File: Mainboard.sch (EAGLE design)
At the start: 80 parts, among them J1 POWER_JACKPTH_LOCK, T1 MOSFET_PCHAN_20A, T10 SINGLE_NCHAN_FET, T2 SINGLE_NCHAN_FET, T3 MOSFET_PCHAN_20A, T4 SINGLE_NCHAN_FET, T5 MOSFET_PCHAN_20A, T6 SINGLE_NCHAN_FET, T7 MOSFET_PCHAN_20A, T8 SINGLE_NCHAN_FET, T9 MOSFET_PCHAN_20A, U1 RFM23BP, U2 ARDUINO_PRO_MINI, U3 HMC5883LSMD, U4 TEENSY_3.0+4, U5 ITG-3200, U6 CURRENT_MAX4372, U7 MURATA_REG_OKL-T3-W12, U8 CURRENT_MAX4372

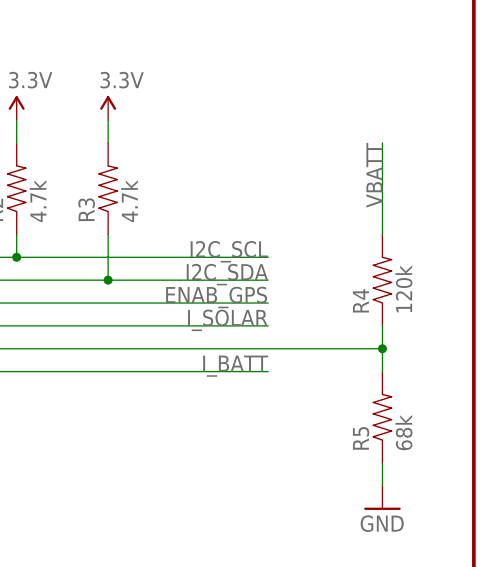
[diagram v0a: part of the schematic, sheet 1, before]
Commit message: Changed R4 value on mainboard
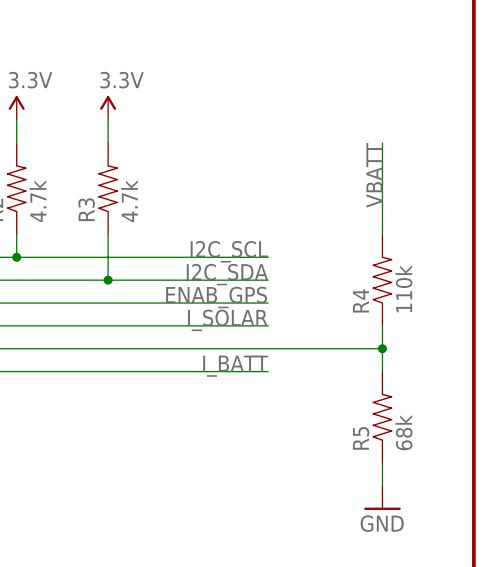
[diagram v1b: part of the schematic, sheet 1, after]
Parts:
- R4: value 120k -> 110k
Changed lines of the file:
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@@
 <part name="P+4" library="SparkFun" deviceset="3.3V" device=""/>
 <part name="P+6" library="SparkFun" deviceset="3.3V" device=""/>
-<part name="R4" library="SparkFun-Resistors" deviceset="RESISTOR" device="0805-RES" value="120k"/>
+<part name="R4" library="SparkFun-Resistors" deviceset="RESISTOR" device="0805-RES" value="110k"/>
 <part name="R5" library="SparkFun-Resistors" deviceset="RESISTOR" device="0805-RES" value="68k"/>
 <part name="GND28" library="SparkFun" deviceset="GND" device=""/>

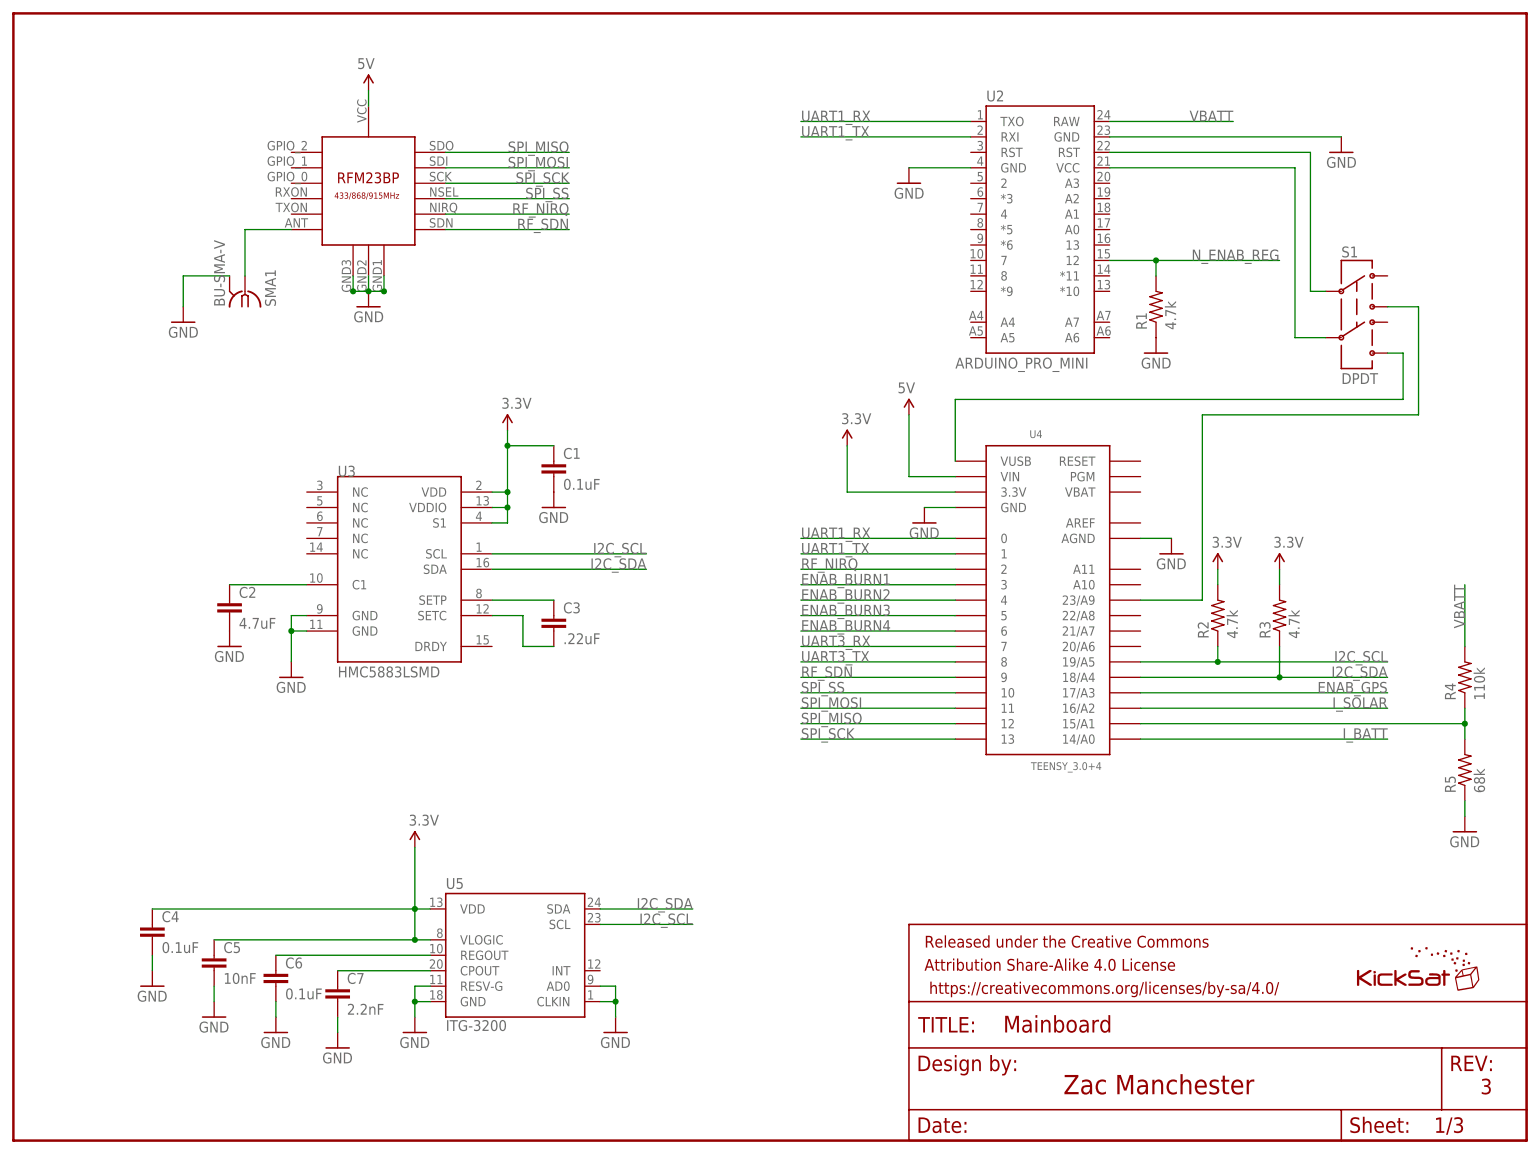
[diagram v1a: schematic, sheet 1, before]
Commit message: Added cap to battery voltage divider ADC input
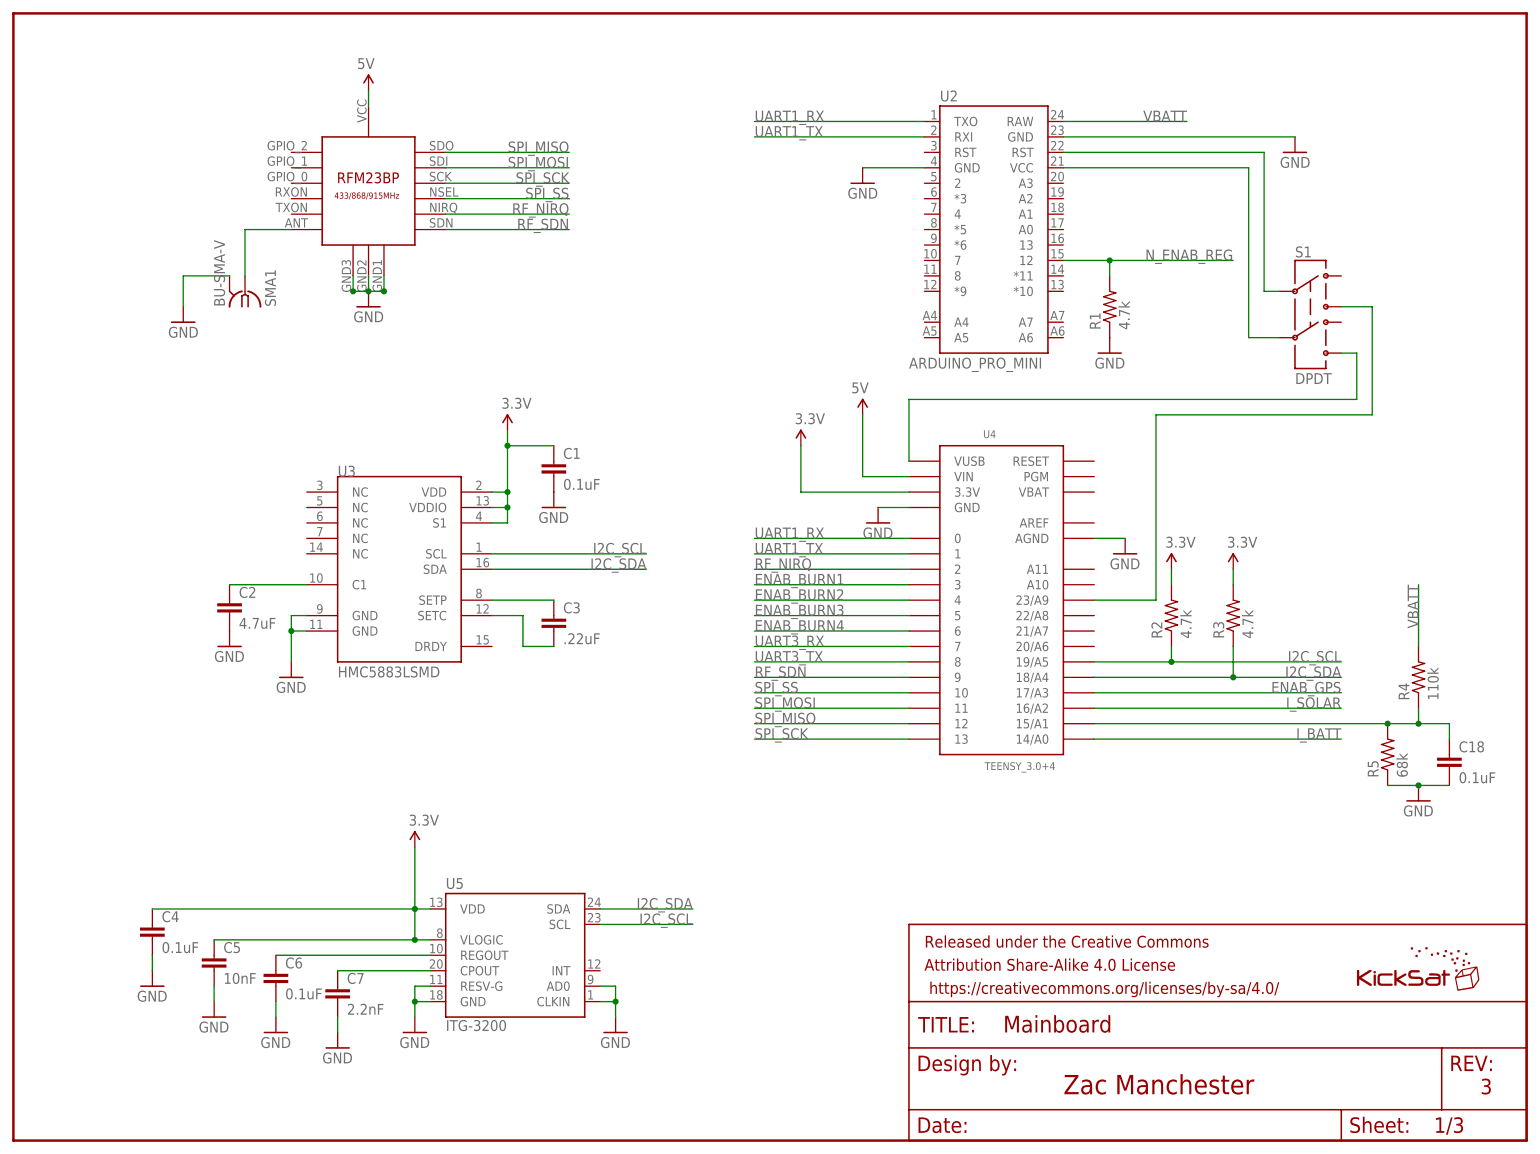
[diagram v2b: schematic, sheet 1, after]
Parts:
- added C18: 0.1uF, SparkFun-Capacitors:CAP0805
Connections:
- net GND: now also C18.2
- net N$37: now also C18.1
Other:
- moved on the sheet: R1, R2, R3, R4, R5, S1, U2, U4

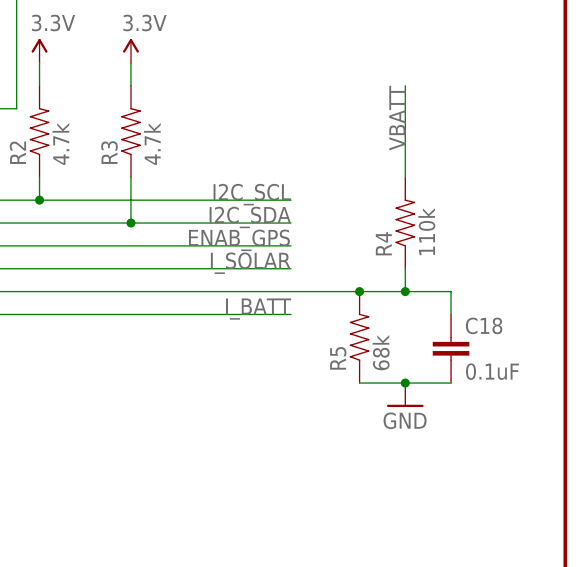
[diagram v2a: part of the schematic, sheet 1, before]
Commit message: Changed voltage divider resistor values
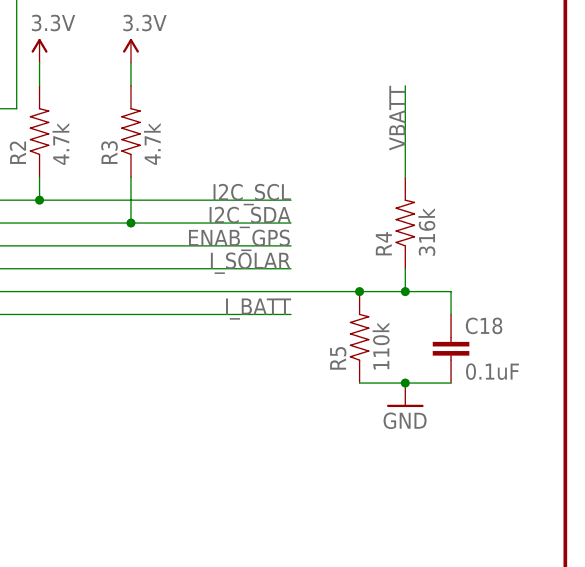
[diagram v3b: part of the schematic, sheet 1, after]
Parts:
- R4: value 110k -> 316k
- R5: value 68k -> 110k
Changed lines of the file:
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@@
 <part name="P+4" library="SparkFun" deviceset="3.3V" device=""/>
 <part name="P+6" library="SparkFun" deviceset="3.3V" device=""/>
-<part name="R4" library="SparkFun-Resistors" deviceset="RESISTOR" device="0805-RES" value="110k"/>
-<part name="R5" library="SparkFun-Resistors" deviceset="RESISTOR" device="0805-RES" value="68k"/>
+<part name="R4" library="SparkFun-Resistors" deviceset="RESISTOR" device="0805-RES" value="316k"/>
+<part name="R5" library="SparkFun-Resistors" deviceset="RESISTOR" device="0805-RES" value="110k"/>
 <part name="GND28" library="SparkFun" deviceset="GND" device=""/>
 <part name="P+8" library="SparkFun" deviceset="3.3V" device=""/>

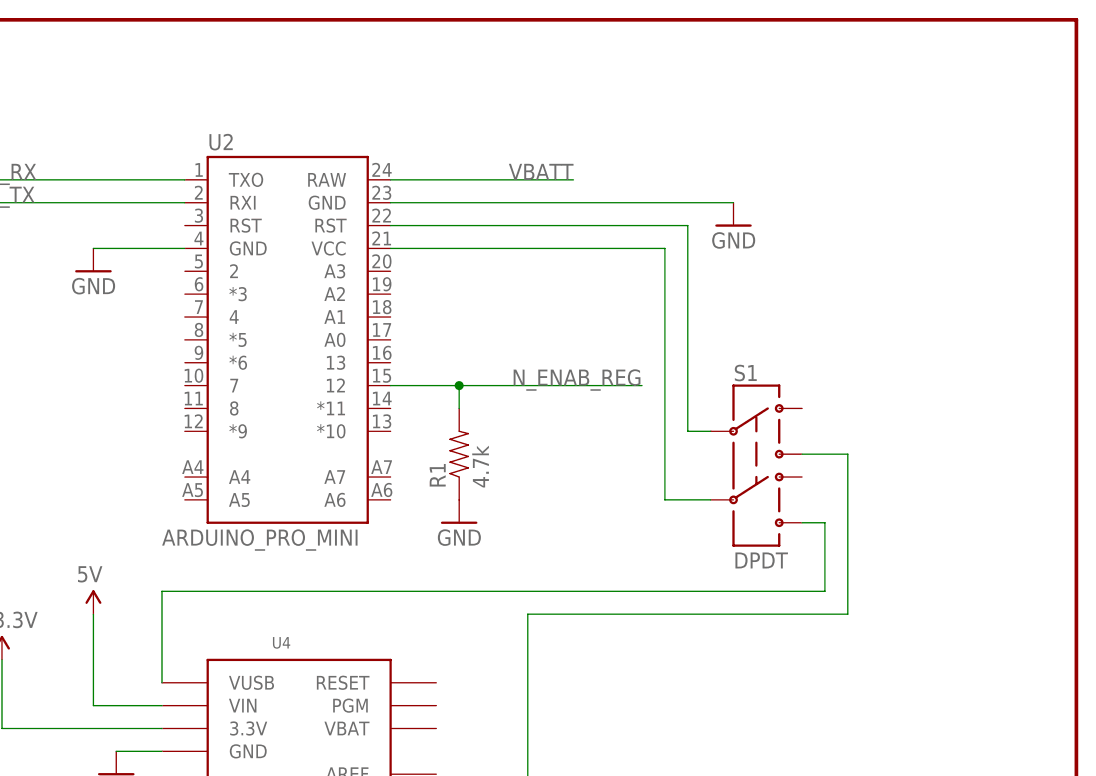
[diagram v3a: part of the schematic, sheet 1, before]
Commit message: Added battery voltage monitoring to arduino
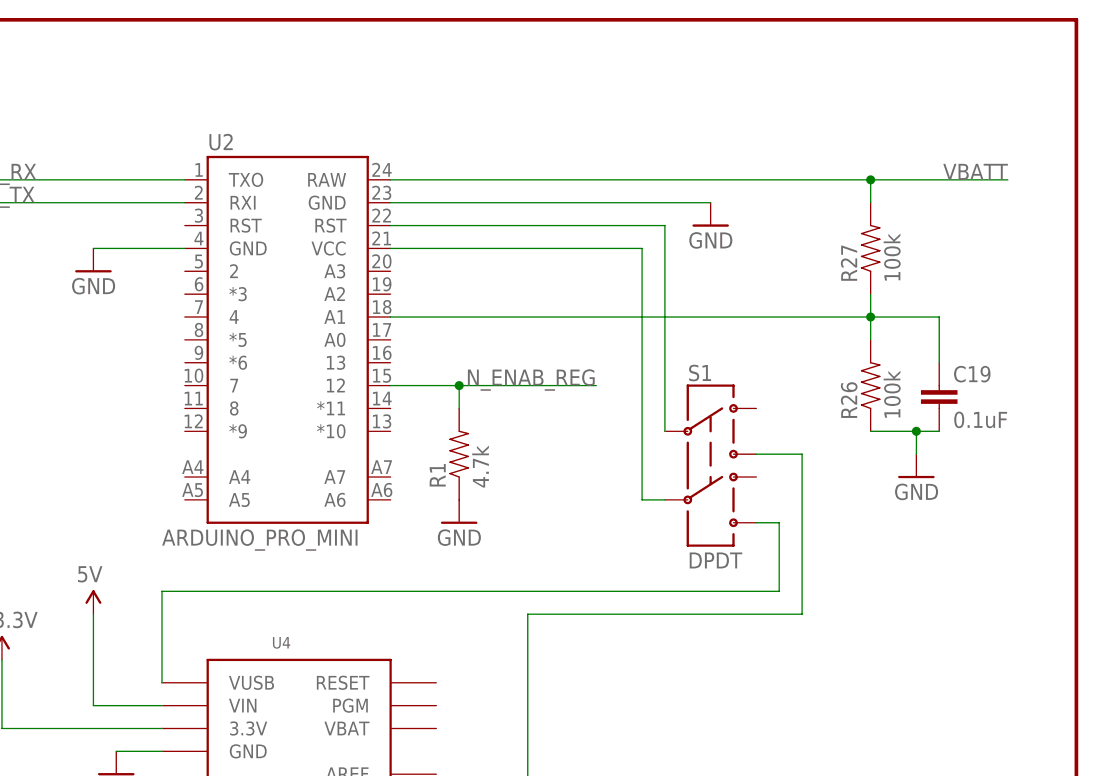
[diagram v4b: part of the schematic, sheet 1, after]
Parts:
- added C19: 0.1uF, SparkFun-Capacitors:CAP0805
- added R26, R27: 100k, SparkFun-Resistors:RESISTOR0805-RES
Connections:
- new net N$17: C19.1, R26.2, R27.1, U2.A1
- net GND: now also C19.2, R26.1
- net VBATT: now also R27.2
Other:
- moved on the sheet: S1
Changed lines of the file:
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@@
 <part name="U$3" library="KickSat-Logo" deviceset="KICKSAT_LOGO" device=""/>
 <part name="C18" library="SparkFun-Capacitors" deviceset="CAP" device="0805" value="0.1uF"/>
+<part name="R26" library="SparkFun-Resistors" deviceset="RESISTOR" device="0805-RES" value="100k"/>
+<part name="R27" library="SparkFun-Resistors" deviceset="RESISTOR" device="0805-RES" value="100k"/>
+<part name="C19" library="SparkFun-Capacitors" deviceset="CAP" device="0805" value="0.1uF"/>
+<part name="GND27" library="SparkFun" deviceset="GND" device=""/>
 </parts>
 <sheets>
@@
 <instance part="P+3" gate="G$1" x="129.54" y="114.3"/>
 <instance part="SUPPLY1" gate="G$1" x="139.7" y="119.38" rot="MR0"/>
-<instance part="GND14" gate="1" x="210.82" y="162.56" rot="MR0"/>
+<instance part="GND14" gate="1" x="208.28" y="162.56" rot="MR0"/>
 <instance part="GND18" gate="1" x="139.7" y="157.48" rot="MR0"/>
 <instance part="U2" gate="G$1" x="160.02" y="152.4" smashed="yes">
@@
 <instance part="R1" gate="G$1" x="180.34" y="137.16" rot="R90"/>
 <instance part="GND19" gate="1" x="180.34" y="129.54" rot="MR0"/>
-<instance part="S1" gate="G$1" x="213.36" y="137.16"/>
+<instance part="S1" gate="G$1" x="208.28" y="137.16"/>
 <instance part="FRAME1" gate="G$1" x="0" y="0"/>
 <instance part="FRAME1" gate="G$2" x="147.32" y="0"/>
 <instance part="U$3" gate="G$1" x="220.98" y="25.4"/>
 <instance part="C18" gate="G$1" x="236.22" y="60.96"/>
+<instance part="R26" gate="G$1" x="226.06" y="144.78" rot="R90"/>
+<instance part="R27" gate="G$1" x="226.06" y="160.02" rot="R90"/>
+<instance part="C19" gate="G$1" x="233.68" y="142.24"/>
+<instance part="GND27" gate="1" x="231.14" y="134.62" rot="MR0"/>
 </instances>
 <busses>
@@
 <segment>
 <pinref part="GND14" gate="1" pin="GND"/>
-<wire x1="172.72" y1="165.1" x2="210.82" y2="165.1" width="0.1524" layer="91"/>
+<wire x1="172.72" y1="165.1" x2="208.28" y2="165.1" width="0.1524" layer="91"/>
 <pinref part="U2" gate="G$1" pin="GND@2"/>
 </segment>
@@
 <wire x1="231.14" y1="58.42" x2="236.22" y2="58.42" width="0.1524" layer="91"/>
 <junction x="231.14" y="58.42"/>
+</segment>
+<segment>
+<pinref part="R26" gate="G$1" pin="1"/>
+<pinref part="C19" gate="G$1" pin="2"/>
+<wire x1="226.06" y1="139.7" x2="231.14" y2="139.7" width="0.1524" layer="91"/>
+<pinref part="GND27" gate="1" pin="GND"/>
+<wire x1="231.14" y1="139.7" x2="233.68" y2="139.7" width="0.1524" layer="91"/>
+<wire x1="231.14" y1="137.16" x2="231.14" y2="139.7" width="0.1524" layer="91"/>
+<junction x="231.14" y="139.7"/>
 </segment>
 </net>
@@
 </segment>
 <segment>
-<wire x1="172.72" y1="167.64" x2="193.04" y2="167.64" width="0.1524" layer="91"/>
-<label x="193.04" y="167.64" size="1.778" layer="95" rot="MR0"/>
+<label x="241.3" y="167.64" size="1.778" layer="95" rot="MR0"/>
 <pinref part="U2" gate="G$1" pin="RAW"/>
+<pinref part="R27" gate="G$1" pin="2"/>
+<wire x1="172.72" y1="167.64" x2="226.06" y2="167.64" width="0.1524" layer="91"/>
+<wire x1="226.06" y1="167.64" x2="226.06" y2="165.1" width="0.1524" layer="91"/>
+<wire x1="226.06" y1="167.64" x2="241.3" y2="167.64" width="0.1524" layer="91"/>
+<junction x="226.06" y="167.64"/>
 </segment>
 </net>
@@
 <segment>
 <pinref part="U2" gate="G$1" pin="VCC"/>
-<wire x1="172.72" y1="160.02" x2="203.2" y2="160.02" width="0.1524" layer="91"/>
-<wire x1="203.2" y1="160.02" x2="203.2" y2="132.08" width="0.1524" layer="91"/>
-<wire x1="208.28" y1="132.08" x2="203.2" y2="132.08" width="0.1524" layer="91"/>
+<wire x1="172.72" y1="160.02" x2="200.66" y2="160.02" width="0.1524" layer="91"/>
+<wire x1="200.66" y1="160.02" x2="200.66" y2="132.08" width="0.1524" layer="91"/>
+<wire x1="203.2" y1="132.08" x2="200.66" y2="132.08" width="0.1524" layer="91"/>
 <pinref part="S1" gate="G$1" pin="5"/>
 </segment>
@@
 <pinref part="U4" gate="G$1" pin="23/A9"/>
 <wire x1="187.96" y1="88.9" x2="177.8" y2="88.9" width="0.1524" layer="91"/>
-<wire x1="187.96" y1="119.38" x2="223.52" y2="119.38" width="0.1524" layer="91"/>
+<wire x1="187.96" y1="119.38" x2="218.44" y2="119.38" width="0.1524" layer="91"/>
 <pinref part="S1" gate="G$1" pin="3"/>
-<wire x1="218.44" y1="137.16" x2="223.52" y2="137.16" width="0.1524" layer="91"/>
-<wire x1="223.52" y1="137.16" x2="223.52" y2="119.38" width="0.1524" layer="91"/>
+<wire x1="213.36" y1="137.16" x2="218.44" y2="137.16" width="0.1524" layer="91"/>
+<wire x1="218.44" y1="137.16" x2="218.44" y2="119.38" width="0.1524" layer="91"/>
 </segment>
 </net>
@@
 <segment>
 <pinref part="U2" gate="G$1" pin="RST@2"/>
-<wire x1="172.72" y1="162.56" x2="205.74" y2="162.56" width="0.1524" layer="91"/>
-<wire x1="205.74" y1="162.56" x2="205.74" y2="139.7" width="0.1524" layer="91"/>
-<wire x1="205.74" y1="139.7" x2="208.28" y2="139.7" width="0.1524" layer="91"/>
+<wire x1="172.72" y1="162.56" x2="203.2" y2="162.56" width="0.1524" layer="91"/>
+<wire x1="203.2" y1="162.56" x2="203.2" y2="139.7" width="0.1524" layer="91"/>
 <pinref part="S1" gate="G$1" pin="2"/>
 </segment>
@@
 <pinref part="U4" gate="G$1" pin="VUSB"/>
 <wire x1="147.32" y1="121.92" x2="147.32" y2="111.76" width="0.1524" layer="91"/>
-<wire x1="147.32" y1="121.92" x2="220.98" y2="121.92" width="0.1524" layer="91"/>
+<wire x1="147.32" y1="121.92" x2="215.9" y2="121.92" width="0.1524" layer="91"/>
 <pinref part="S1" gate="G$1" pin="6"/>
-<wire x1="218.44" y1="129.54" x2="220.98" y2="129.54" width="0.1524" layer="91"/>
-<wire x1="220.98" y1="129.54" x2="220.98" y2="121.92" width="0.1524" layer="91"/>
+<wire x1="213.36" y1="129.54" x2="215.9" y2="129.54" width="0.1524" layer="91"/>
+<wire x1="215.9" y1="129.54" x2="215.9" y2="121.92" width="0.1524" layer="91"/>
 </segment>
 </net>
@@
 <wire x1="172.72" y1="144.78" x2="180.34" y2="144.78" width="0.1524" layer="91"/>
 <pinref part="R1" gate="G$1" pin="2"/>
-<wire x1="180.34" y1="144.78" x2="200.66" y2="144.78" width="0.1524" layer="91"/>
+<wire x1="180.34" y1="144.78" x2="195.58" y2="144.78" width="0.1524" layer="91"/>
 <wire x1="180.34" y1="142.24" x2="180.34" y2="144.78" width="0.1524" layer="91"/>
-<label x="200.66" y="144.78" size="1.778" layer="95" rot="MR0"/>
+<label x="195.58" y="144.78" size="1.778" layer="95" rot="MR0"/>
 <junction x="180.34" y="144.78"/>
 </segment>
 </net>
+<net name="N$17" class="0">
+<segment>
+<pinref part="U2" gate="G$1" pin="A1"/>
+<wire x1="172.72" y1="152.4" x2="226.06" y2="152.4" width="0.1524" layer="91"/>
+<pinref part="C19" gate="G$1" pin="1"/>
+<wire x1="233.68" y1="152.4" x2="233.68" y2="147.32" width="0.1524" layer="91"/>
+<pinref part="R27" gate="G$1" pin="1"/>
+<pinref part="R26" gate="G$1" pin="2"/>
+<wire x1="226.06" y1="149.86" x2="226.06" y2="152.4" width="0.1524" layer="91"/>
+<wire x1="226.06" y1="152.4" x2="226.06" y2="154.94" width="0.1524" layer="91"/>
+<wire x1="233.68" y1="152.4" x2="226.06" y2="152.4" width="0.1524" layer="91"/>
+<junction x="226.06" y="152.4"/>
+</segment>
+</net>
